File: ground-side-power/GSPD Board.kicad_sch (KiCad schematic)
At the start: 34 parts, among them J2 Battery Terminals, J4 Battery Terminals, J5 Battery Terminals, J6 Battery Terminals, SW1 23A, SW2 SW_SPDT, U2 URB2424LD-20WR3

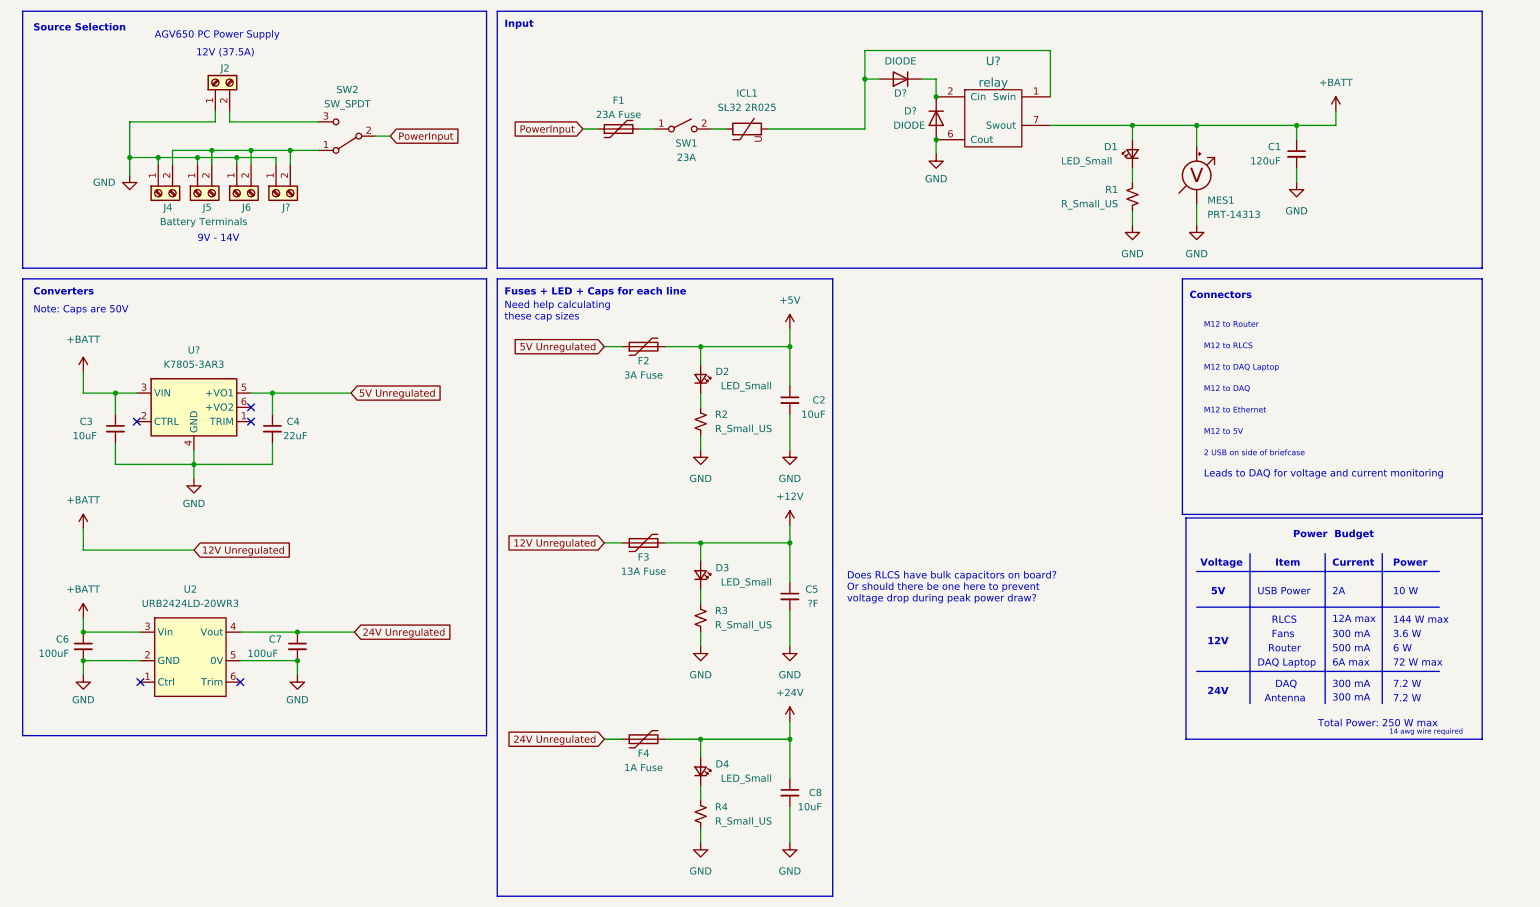
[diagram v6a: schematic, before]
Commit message: Added Relay + Minor Changes
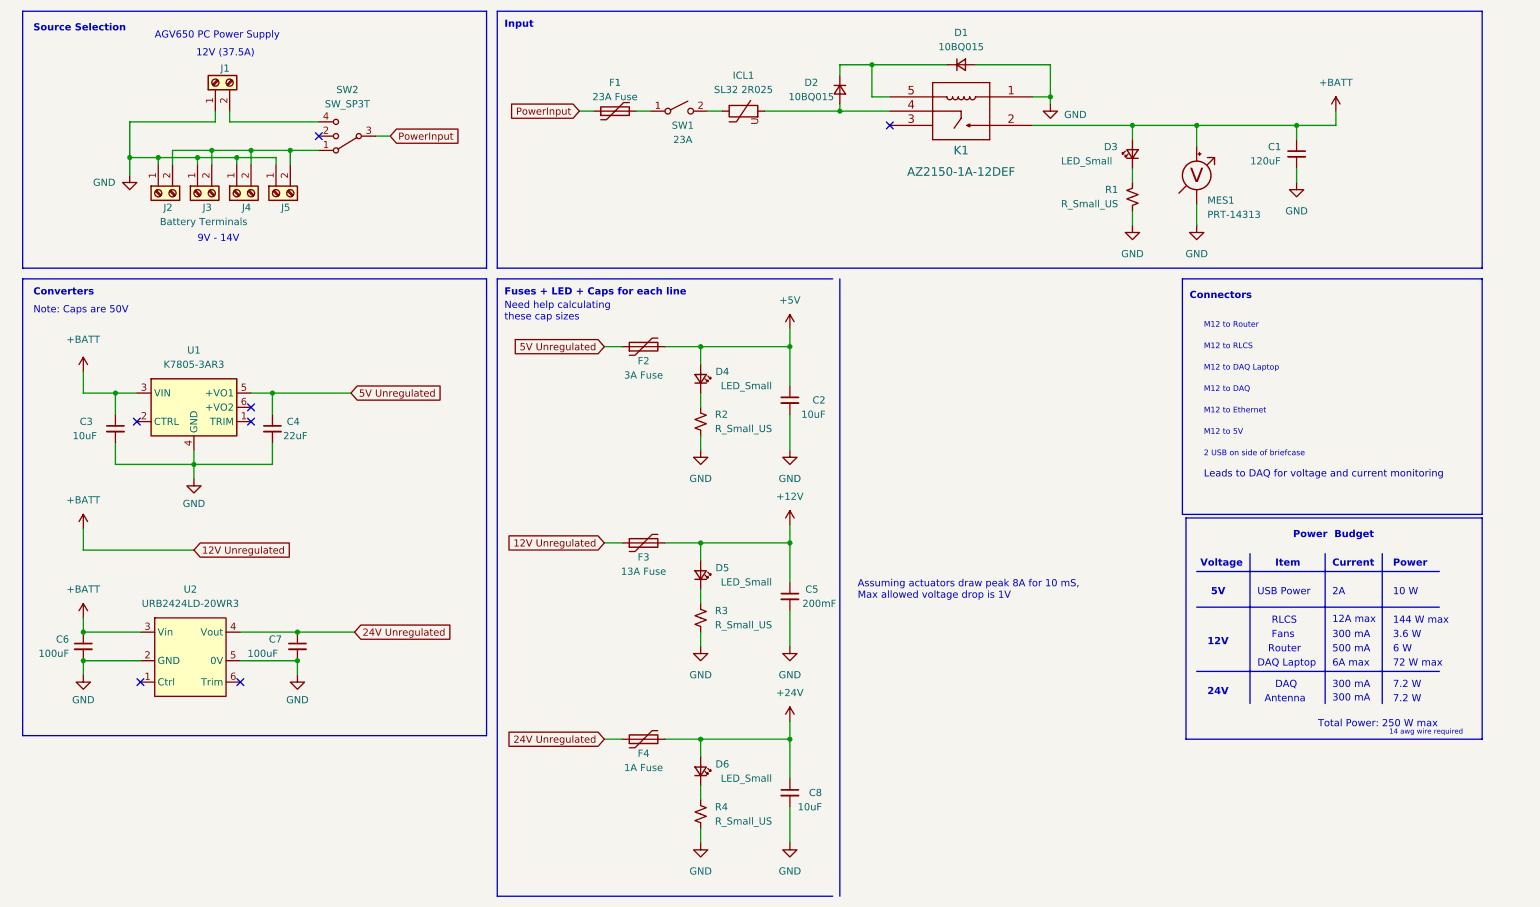
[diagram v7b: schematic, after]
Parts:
- removed D? (x2): DIODE, symbol Simulation_SPICE:DIODE
- removed SW2: SW_SPDT, symbol Switch:SW_SPDT
- removed U?: relay, symbol custom:relay
- added D1, D2: 10BQ015, symbol Device:D_Small
- added K1: AZ2150-1A-12DEF, AZ2150_AMZ, symbol GSP:AZ2150-1A-12DEF
- added SW2: SW_SP3T, symbol Switch:SW_SP3T
- C5: value ?F -> 200mF
- gave numbers to parts that had none: 2
- renumbered D1 to D3, D2 to D4, D3 to D5, D4 to D6, J2 to J1, J4 to J2, J5 to J3, J6 to J4
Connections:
- net +BATT: now also K1.2
- net GND: now also D1.2 (A), K1.1
- net PowerInput: now also SW2.3
- net at J2.2 (Pin_2), J3.2 (Pin_2), J4.2 (Pin_2)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: now also SW2.1
- net at ICL1.2: now also D2.2 (A), K1.4
- net at J1.2 (Pin_2): now also SW2.4
- new net: D1.1 (K), D2.1 (K), K1.5
- no-connect marks 5 -> 7
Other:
- note added: "Assuming actuators draw peak 8A for 10 mS, Max allowed voltage drop is 1V"
- note removed: "Does RLCS have bulk capacitors on board? Or should there be one here to prevent voltage drop during peak power draw?"
- moved on the sheet: F1, ICL1, SW1
